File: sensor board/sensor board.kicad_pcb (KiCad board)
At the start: 2 copper layers, 15.6 x 11.4 mm, 25 parts, among them IC1 AD5933YRSZ, IC2 MAX86141ENP+, J1 502078-1710

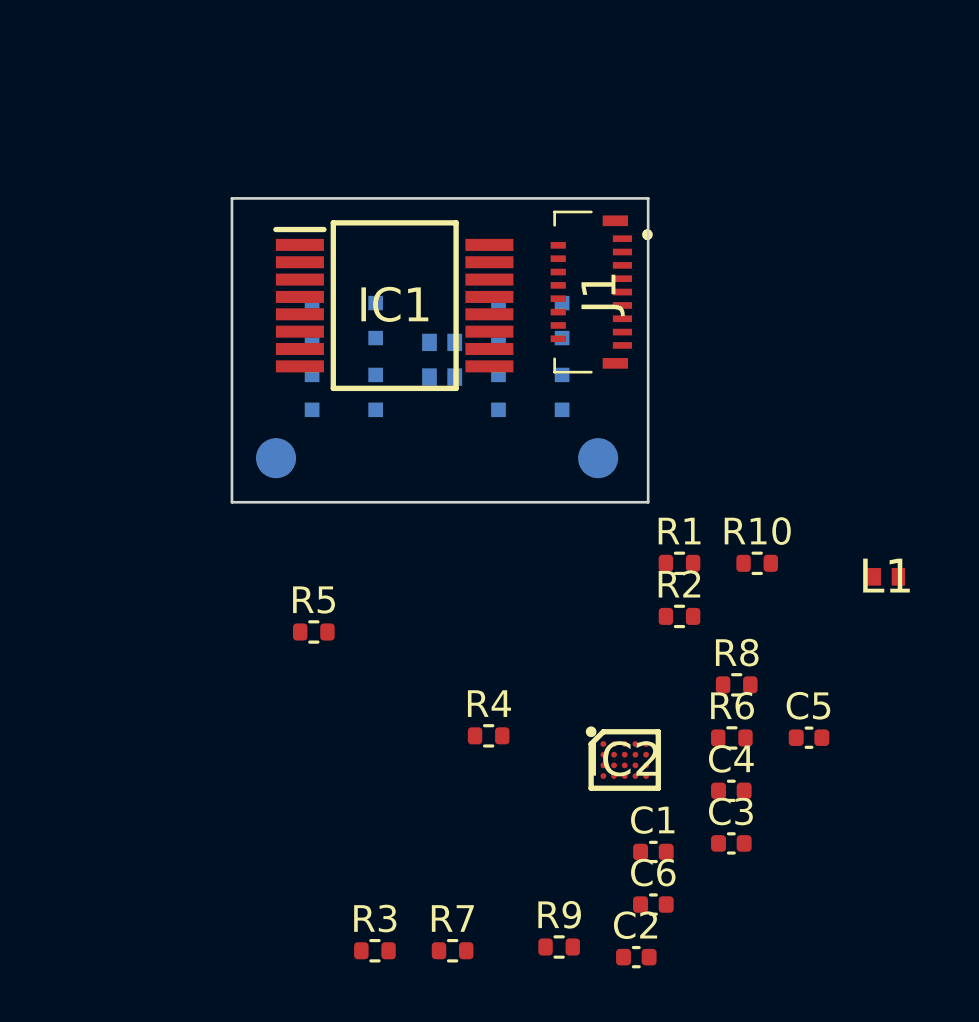
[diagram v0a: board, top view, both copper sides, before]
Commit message: updated sensor board size created netlist for main board
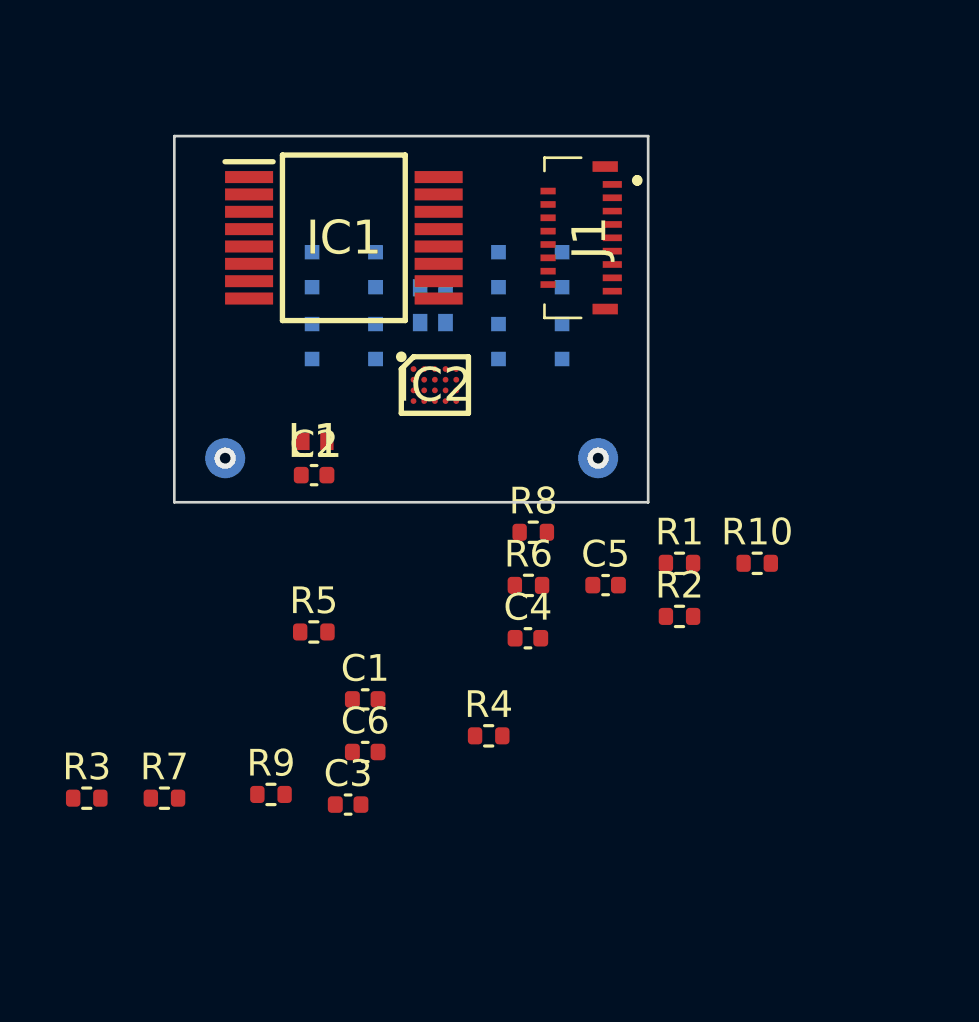
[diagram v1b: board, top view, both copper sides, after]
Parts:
- moved L1 22.0 mm to (136.7, 82.5)
- moved C2 20.8 mm to (136.7, 83.8)
- moved IC2 15.7 mm to (141.2, 80.4)
- moved C1 12.2 mm to (138.6, 92.2)
- moved C6 12.2 mm to (138.6, 94.2)
- moved R3 12.2 mm to (128.2, 95.9)
- moved R7 12.2 mm to (131.1, 95.9)
- moved R9 12.2 mm to (135.1, 95.8)
- moved C3 12.2 mm to (138.0, 96.2)
- moved C5 9.53 mm to (147.6, 87.9)
- moved R6 9.53 mm to (144.7, 88.0)
- moved C4 9.52 mm to (144.7, 89.9)
- moved R8 9.52 mm to (144.9, 86.0)
- moved IC1 3.17 mm to (137.8, 74.9)
- moved D1 2.07 mm to (141.1, 77.5)
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- renumbered C3 to C2, C2 to C3
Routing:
- net Net-(C2-Pad2): vias 0 -> 1
- net Net-(C2-Pad1): vias 0 -> 1
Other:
- board size 15.6 x 11.4 mm -> 17.7 x 13.7 mm
- copper layers 2 -> 4

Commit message: - add components to main board - put sensor contacts in the middle of the side edges
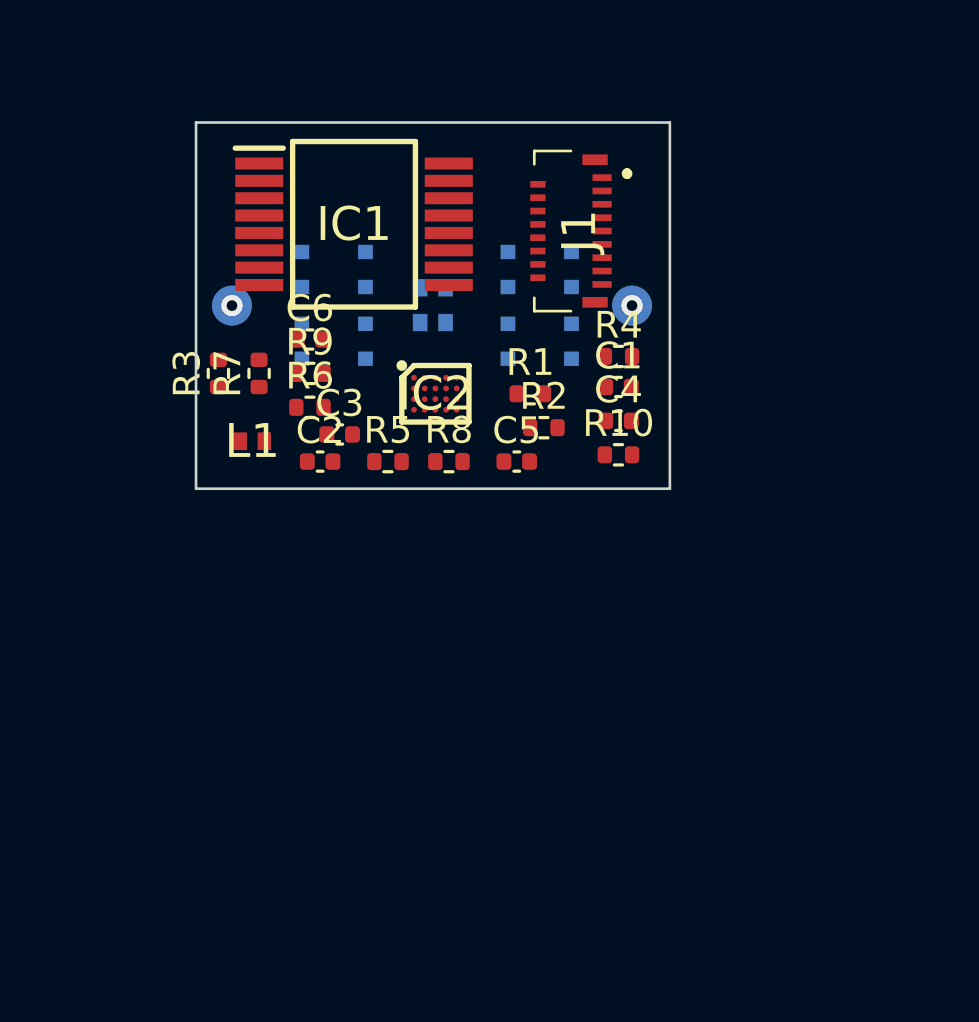
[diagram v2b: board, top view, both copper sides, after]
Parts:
- moved R3 16.7 mm to (133.1, 80.0), turned to 90 degrees
- moved R7 16.3 mm to (134.6, 80.0), turned to 90 degrees
- moved R9 15.8 mm to (136.5, 80.0)
- moved C6 15.6 mm to (136.5, 78.7)
- moved C1 15.1 mm to (148.1, 80.5)
- moved R4 15.0 mm to (148.1, 79.4)
- moved C3 13.9 mm to (137.6, 82.3)
- moved R6 10.6 mm to (136.5, 81.3)
- moved C4 8.82 mm to (148.1, 81.8)
- moved R2 8.71 mm to (145.3, 82.0)
- moved R1 8.46 mm to (144.8, 80.8)
- moved R5 6.96 mm to (139.4, 83.3)
- moved R10 6.60 mm to (148.1, 83.1)
- moved TP1 5.85 mm to (148.6, 77.5)
- moved TP2 5.72 mm to (133.6, 77.5)
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
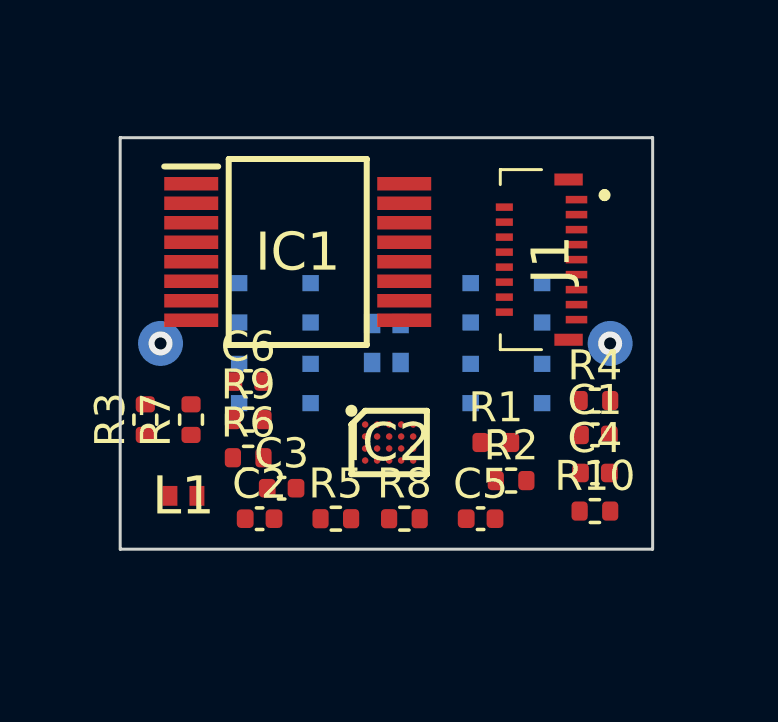
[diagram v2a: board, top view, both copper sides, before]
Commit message: added impedance probe pins
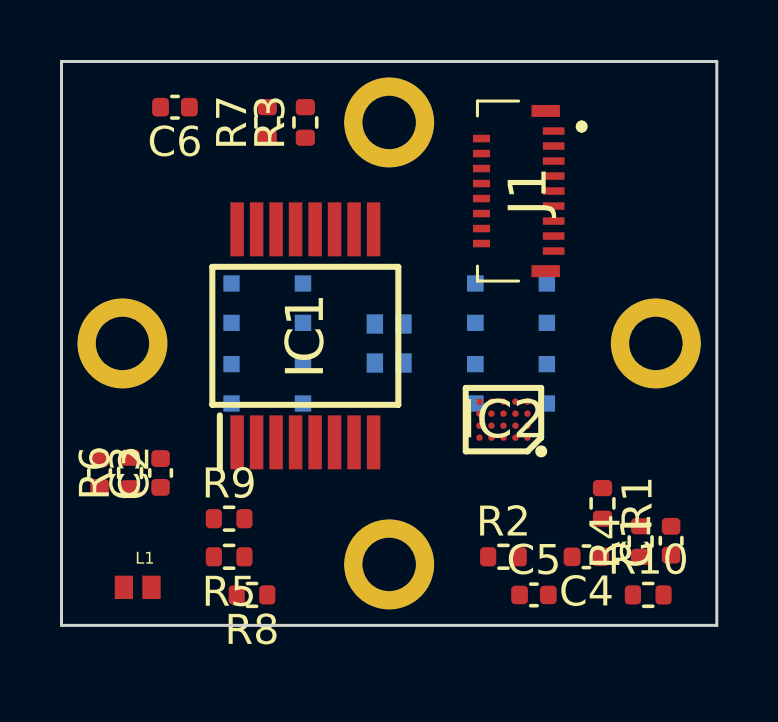
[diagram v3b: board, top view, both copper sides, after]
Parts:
- removed TP1, TP2: TestPoint, TestPoint:TestPoint_Pad_D1.5mm
- added J2: Probe_01_male, Horace:Probe_01_male, B.Cu at (141.2, 84.8)
- added J3: Probe_01_male, Horace:Probe_01_male, B.Cu at (141.2, 70.1)
- added J4: Probe_01_male, Horace:Probe_01_male, B.Cu at (150.1, 77.5)
- added J5: Probe_01_male, Horace:Probe_01_male, B.Cu at (132.3, 77.5)
- L1: footprint Horace:LQW15DN100M00D -> Horace:LQW15DN150M00D
- moved R3 11.3 mm to (138.4, 70.1)
- moved R7 10.2 mm to (137.2, 70.1)
- moved C6 9.46 mm to (134.1, 69.6), turned to 180 degrees
- moved R8 5.68 mm to (136.7, 85.9), turned to 180 degrees
- moved C2 5.55 mm to (131.6, 81.8), turned to 270 degrees
- moved R4 4.94 mm to (149.6, 84.1), turned to 90 degrees
- moved C1 4.35 mm to (150.6, 84.0), turned to 90 degrees
- moved R1 4.09 mm to (148.3, 82.8), turned to 270 degrees
- moved C3 4.07 mm to (133.6, 81.8), turned to 90 degrees
- moved R6 3.97 mm to (132.6, 81.8), turned to 90 degrees
- moved IC2 3.89 mm to (145.0, 80.0), turned to 180 degrees
- moved R5 3.78 mm to (135.9, 84.6), turned to 180 degrees
- moved L1 3.41 mm to (132.8, 85.6)
- moved R9 3.36 mm to (135.9, 83.3)
- moved R10 3.31 mm to (149.9, 85.9)
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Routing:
- net Net-(C2-Pad2): vias 1 -> 0
- net Net-(C2-Pad1): vias 1 -> 0
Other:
- board size 17.7 x 13.7 mm -> 21.8 x 18.8 mm

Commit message: via/nets definition
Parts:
- moved C5 21.1 mm to (132.1, 70.1), turned to 270 degrees
- moved R3 18.0 mm to (150.4, 83.6), turned to 270 degrees
- moved R2 16.1 mm to (137.9, 70.1), turned to 90 degrees
- moved R5 12.6 mm to (132.6, 72.4)
- moved R6 7.38 mm to (132.1, 74.4)
- moved R10 5.80 mm to (144.5, 83.6), turned to 90 degrees
- moved C1 4.09 mm to (146.6, 83.6), turned to 270 degrees
- moved R8 2.54 mm to (138.2, 83.8), turned to 90 degrees
- moved C4 2.40 mm to (145.8, 85.9), turned to 0 degrees
- moved R1 2.39 mm to (149.6, 80.8)
- moved R7 1.27 mm to (135.9, 70.1), turned to 270 degrees
- moved R4 1.14 mm to (148.6, 83.6), turned to 270 degrees
- moved L1 1.05 mm to (133.1, 84.6), turned to 270 degrees
- moved R9 0.57 mm to (136.1, 83.8), turned to 90 degrees
- moved C6 0.56 mm to (133.9, 70.1), turned to 270 degrees
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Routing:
- net (no net): vias 0 -> 6
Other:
- net class sensor added: clearance 0.1, trace_width 0.25, via_dia 0.254, via_drill 0.1
- rule trace_min: 0.2 -> 0.1
- rule via_min_drill: 0.3 -> 0.1
- rule via_min_size: 0.4 -> 0.254

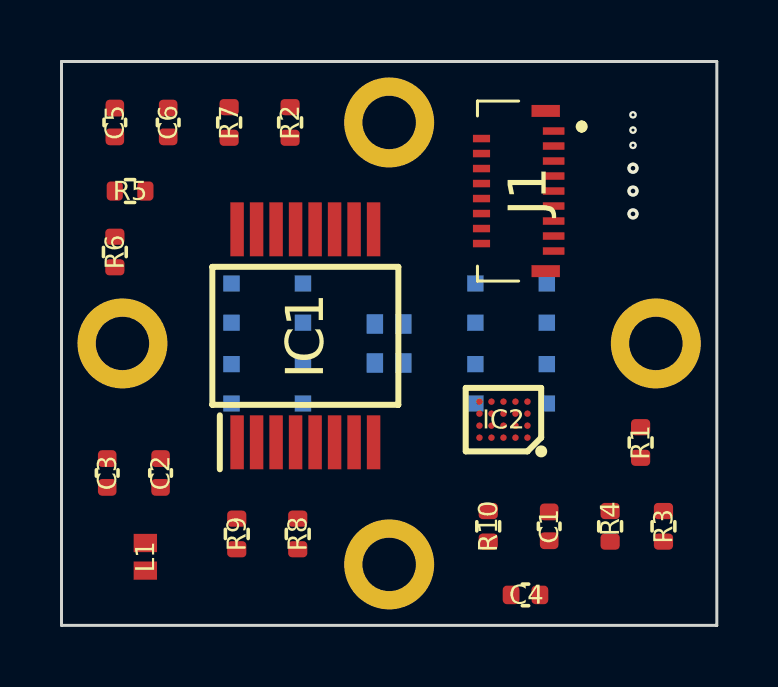
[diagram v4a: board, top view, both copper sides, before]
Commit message: added buried vias
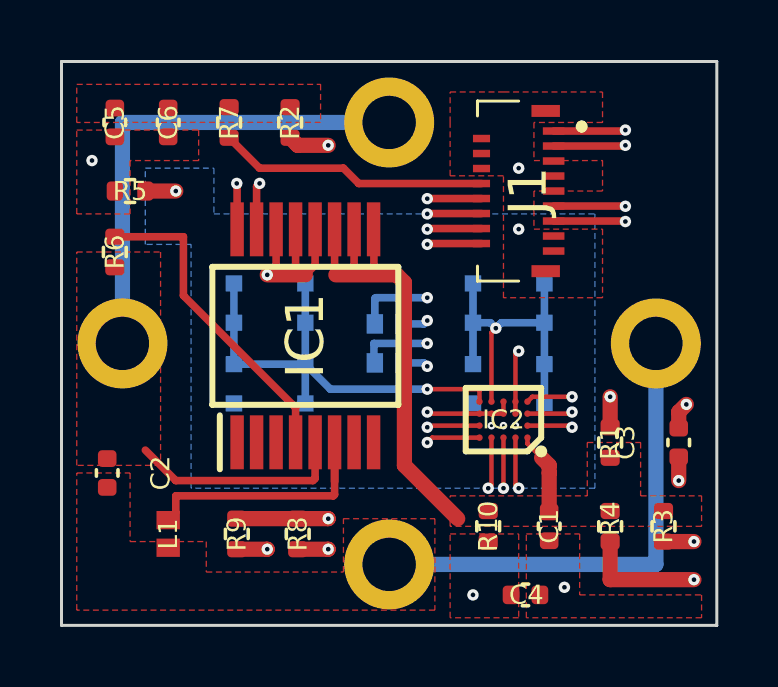
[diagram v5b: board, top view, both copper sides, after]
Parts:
- moved C3 17.3 mm to (150.9, 80.8)
- moved D2 8.05 mm to (137.2, 77.5), turned to 270 degrees
- moved D3 8.05 mm to (145.2, 77.5), turned to 270 degrees
- moved L1 1.08 mm to (133.9, 83.8)
- moved R1 1.02 mm to (148.6, 80.8)
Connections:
- IC2 pad C3: GNDREF -> GNDS
- IC2 pad C4: GNDREF -> GNDS
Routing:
- net Net-(C2-Pad1): track 0.00 -> 23.6 mm
- net +3V3: track 0.00 -> 19.7 mm
- net Net-(C2-Pad2): track 0.00 -> 17.0 mm
- net Net-(D2-Pad1): track 0.00 -> 15.6 mm, vias 0 -> 1
- net /SCLK: track 0.00 -> 15.4 mm, vias 0 -> 2
- net Net-(J1-Pad11): track 0.00 -> 15.3 mm, vias 0 -> 2
- net Net-(D3-Pad1): track 0.00 -> 11.7 mm, vias 0 -> 1
- net Net-(IC1-Pad4): track 0.00 -> 10.7 mm
- net Net-(J1-Pad13): track 0.00 -> 10.5 mm, vias 0 -> 2
- net Net-(IC1-Pad6): track 0.00 -> 9.29 mm
- net /INT: track 0.00 -> 9.04 mm, vias 0 -> 1
- net /SDA: track 0.00 -> 8.03 mm, vias 0 -> 3
- net GNDREF: track 0.00 -> 7.78 mm, vias 0 -> 6
- net +1V8: track 0.00 -> 5.18 mm, vias 0 -> 2
- net /SCL: track 0.00 -> 4.96 mm, vias 0 -> 3
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- added copper zone on F.Cu, net +1V8
- added copper zone on F.Cu, net +3V3
- added copper zone on F.Cu, net GNDREF
- added copper zone on In2.Cu, net GNDREF
- added copper zone on B.Cu, net GNDS
- added copper zone on F.Cu, net Net-(C2-Pad1)
- added copper zone on F.Cu, net Net-(C2-Pad2)
- added copper zone on F.Cu, net Net-(C4-Pad1)
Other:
- net class sensor: trace_width 0.25 -> 0.254

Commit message: finished sensor PCB
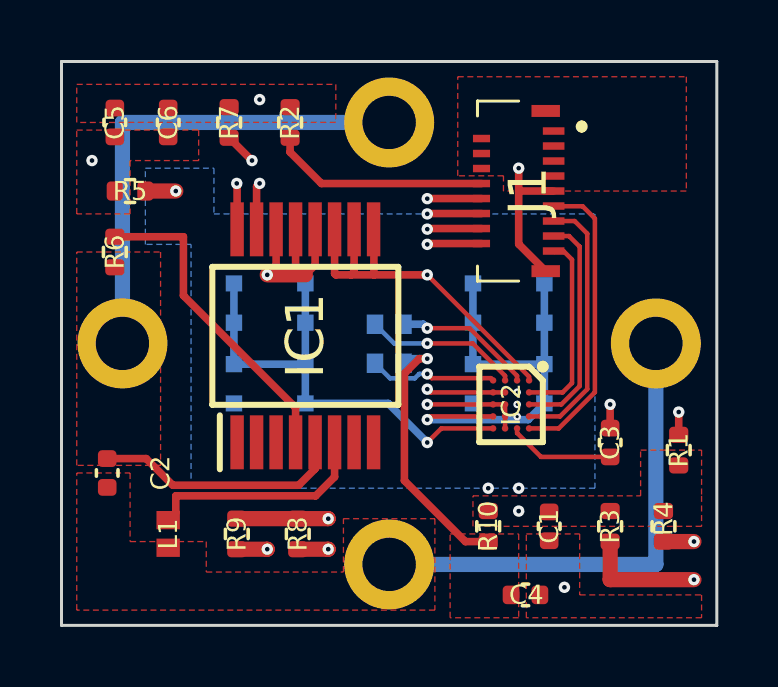
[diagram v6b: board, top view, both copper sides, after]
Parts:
- moved R1 2.30 mm to (150.9, 81.0), turned to 90 degrees
- moved C3 2.29 mm to (148.6, 80.8)
- moved R3 1.78 mm to (148.6, 83.6)
- moved R4 1.78 mm to (150.4, 83.6)
- moved IC2 0.57 mm to (145.3, 79.5), turned to 270 degrees
- turned D1 to 180 degrees
- turned R2 to 270 degrees
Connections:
- J1 pad 1: /SCL -> GNDREF
- J1 pad 10: /CSB -> /INT
- J1 pad 11: Net-(J1-Pad11) -> /CSB
- J1 pad 12: /SDI -> /SDA
- J1 pad 13: Net-(J1-Pad13) -> /SDI
- J1 pad 14: /SDO -> /SCL
- J1 pad 15: GNDREF -> /SDO
- J1 pad 16: /SCLK -> Net-(J1-Pad16)
- J1 pad 17: GNDREF -> /SCLK
- J1 pad 3: /SDA -> GNDREF
- J1 pad 8: /INT -> Net-(J1-Pad8)
- R1 pad 1: Net-(J1-Pad13) -> +3V3
- R1 pad 2: +3V3 -> Net-(J1-Pad16)
- R2 pad 1: Net-(J1-Pad11) -> +1V8
- R2 pad 2: +1V8 -> Net-(J1-Pad8)
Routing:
- net /SCL: track 4.96 -> 29.9 mm
- net +1V8: track 5.18 -> 23.9 mm, vias 2 -> 3
- net /SDA: track 8.03 -> 25.2 mm
- net /INT: track 9.04 -> 25.0 mm, vias 1 -> 3
- net Net-(J1-Pad11): track 15.3 -> 0.00 mm, vias 2 -> 0
- net Net-(J1-Pad16): track 0.00 -> 13.3 mm, vias 0 -> 2
- net Net-(IC2-PadB4): track 1.02 -> 12.0 mm, vias 2 -> 3
- net Net-(J1-Pad13): track 10.5 -> 0.00 mm, vias 2 -> 0
- net Net-(IC2-PadB3): track 1.02 -> 11.4 mm, vias 2 -> 3
- net /SCLK: track 15.4 -> 6.45 mm, vias 2 -> 0
- net Net-(J1-Pad8): track 0.00 -> 7.29 mm
- net Net-(C4-Pad1): track 2.60 -> 9.03 mm, vias 2 -> 1
- net /CSB: track 3.62 -> 10.0 mm, vias 2 -> 0
- net /SDI: track 3.54 -> 8.79 mm, vias 2 -> 0
- net GNDREF: track 7.78 -> 12.6 mm, vias 6 -> 5
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
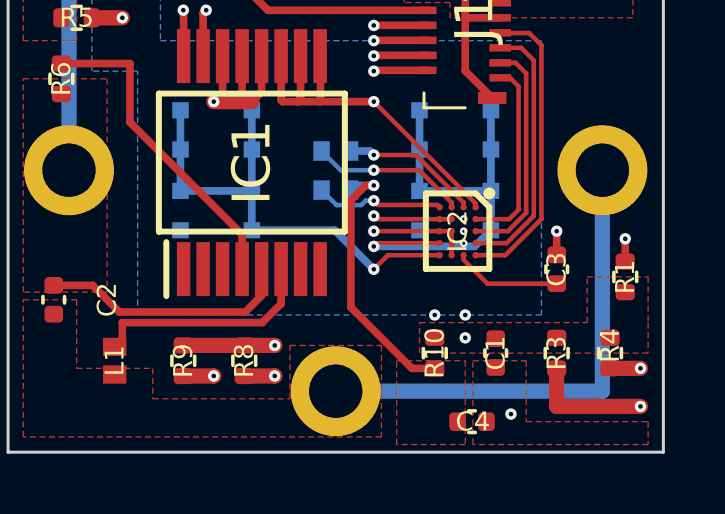
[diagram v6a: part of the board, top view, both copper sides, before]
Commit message: removed unnecessary vias
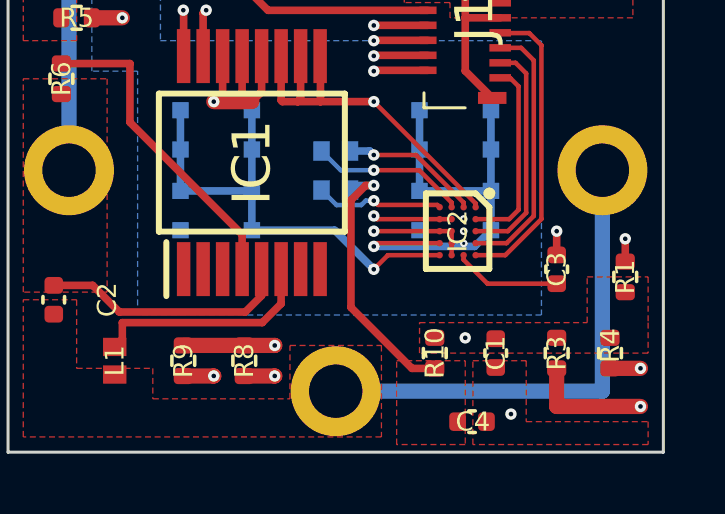
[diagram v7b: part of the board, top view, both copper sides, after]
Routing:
- net Net-(IC2-PadB4): vias 3 -> 2
- net Net-(IC2-PadB3): vias 3 -> 2

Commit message: replaced probe wire with zone
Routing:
- net Net-(C2-Pad2): track 17.0 -> 0.76 mm
- net Net-(C2-Pad1): track 24.7 -> 8.41 mm
- added copper zone on B.Cu, net Net-(C2-Pad1)
- added copper zone on B.Cu, net Net-(C2-Pad2)
